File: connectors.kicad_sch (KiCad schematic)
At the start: 1 part, among them J1 USB_C_Receptacle_USB2.0_14P

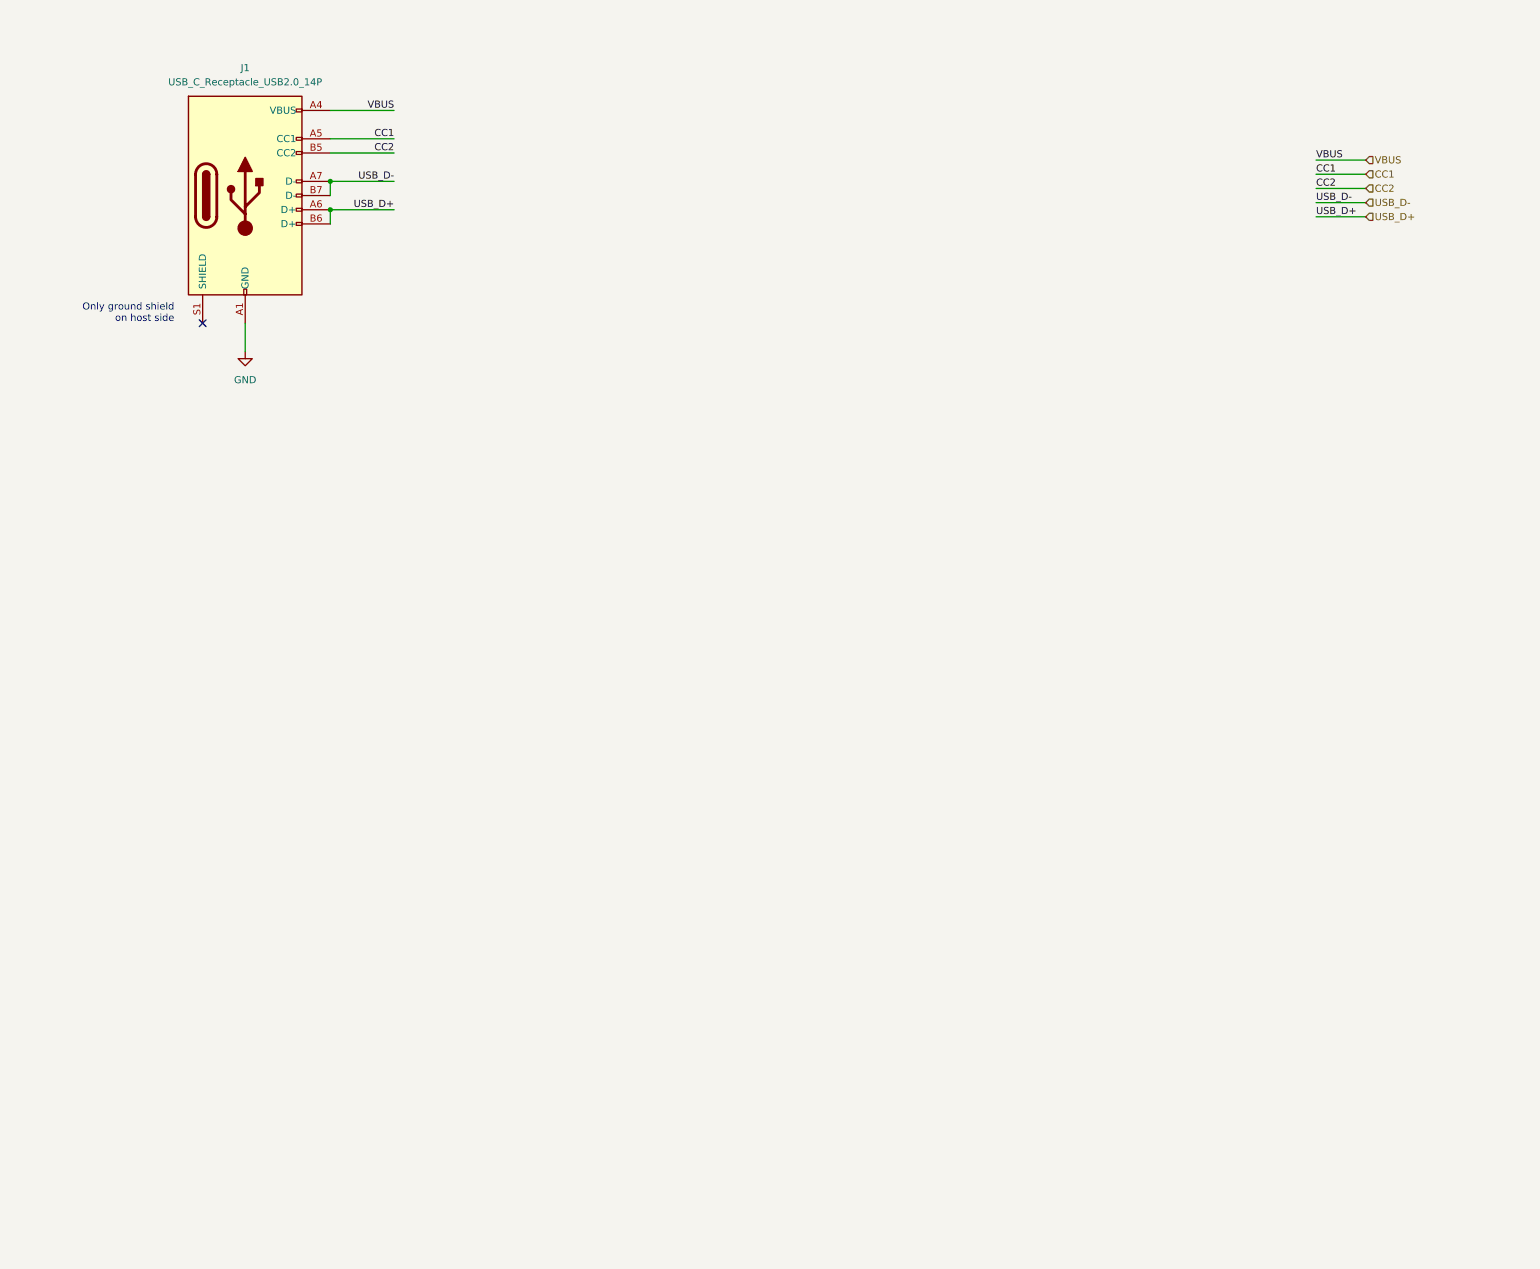
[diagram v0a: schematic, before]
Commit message: Add ESP32-S3-WROOM-1, 5V rail and UI sheet
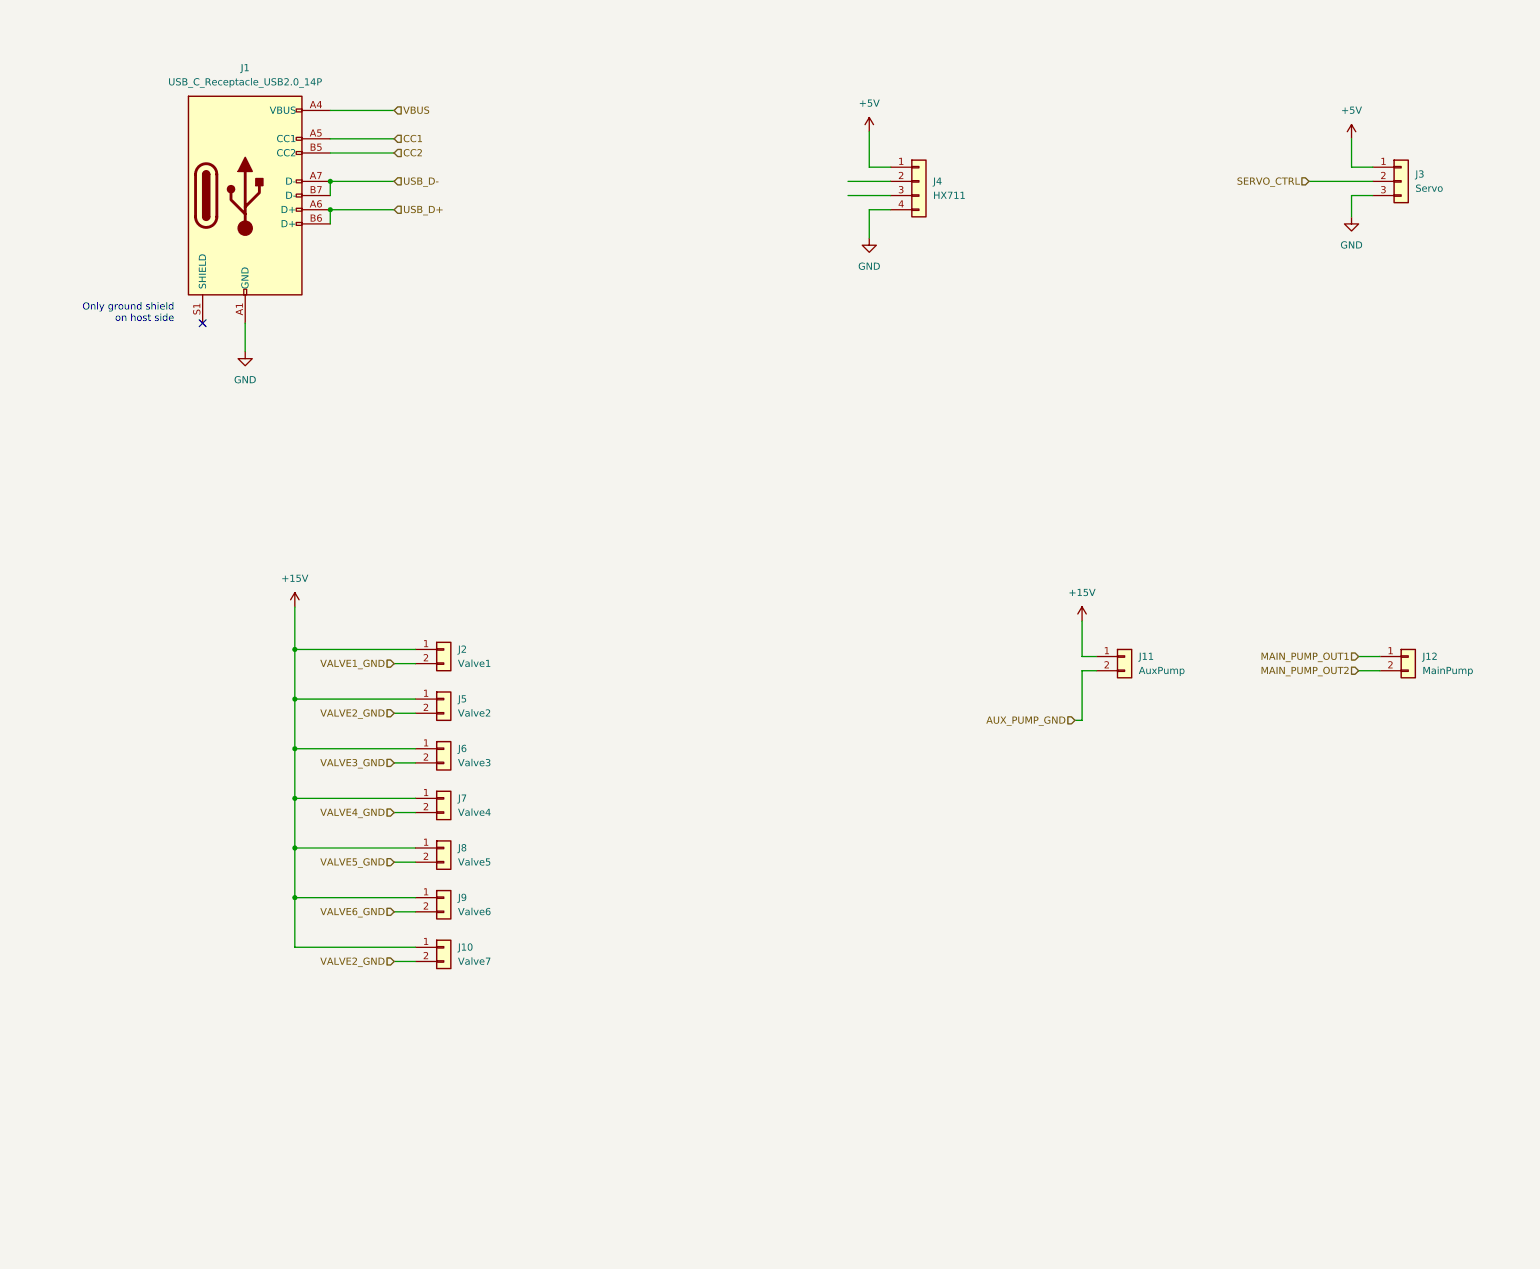
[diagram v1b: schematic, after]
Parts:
- added J10: Valve7, symbol Connector_Generic:Conn_01x02
- added J11: AuxPump, symbol Connector_Generic:Conn_01x02
- added J12: MainPump, symbol Connector_Generic:Conn_01x02
- added J2: Valve1, symbol Connector_Generic:Conn_01x02
- added J3: Servo, symbol Connector_Generic:Conn_01x03
- added J4: HX711, symbol Connector_Generic:Conn_01x04
- added J5: Valve2, symbol Connector_Generic:Conn_01x02
- added J6: Valve3, symbol Connector_Generic:Conn_01x02
- added J7: Valve4, symbol Connector_Generic:Conn_01x02
- added J8: Valve5, symbol Connector_Generic:Conn_01x02
- added J9: Valve6, symbol Connector_Generic:Conn_01x02
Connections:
- net GND: now also J3.3 (Pin_3), J4.4 (Pin_4)
- new net +15V: J10.1 (Pin_1), J11.1 (Pin_1), J2.1 (Pin_1), J5.1 (Pin_1), J6.1 (Pin_1), J7.1 (Pin_1), J8.1 (Pin_1), J9.1 (Pin_1)
- new net +5V: J3.1 (Pin_1), J4.1 (Pin_1)
- new net AUX_PUMP_GND: J11.2 (Pin_2)
- new net MAIN_PUMP_OUT1: J12.1 (Pin_1)
- new net MAIN_PUMP_OUT2: J12.2 (Pin_2)
- new net SERVO_CTRL: J3.2 (Pin_2)
- new net VALVE1_GND: J2.2 (Pin_2)
- new net VALVE2_GND: J10.2 (Pin_2), J5.2 (Pin_2)
- new net VALVE3_GND: J6.2 (Pin_2)
- new net VALVE4_GND: J7.2 (Pin_2)
- new net VALVE5_GND: J8.2 (Pin_2)
- new net VALVE6_GND: J9.2 (Pin_2)

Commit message: Finish first design
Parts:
- removed J1: USB_C_Receptacle_USB2.0_14P, symbol Connector:USB_C_Receptacle_USB2.0_14P
- added J1: USB_C_Receptacle_USB2.0_16P, project:USB_C_Receptacle_JAE_DX07S016JA1R1500, symbol Connector:USB_C_Receptacle_USB2.0_16P
- added J13: WaterLevelSensor, Connector_JST:JST_XH_B2B-XH-A_1x02_P2.50mm_Vertical, symbol Connector_Generic:Conn_01x02
- added J14: Conn_01x04, Connector_PinHeader_2.54mm:PinHeader_1x04_P2.54mm_Vertical, symbol Connector_Generic:Conn_01x04
- J10, J11, J12, J2, J5, J6, J7, J8, J9: footprint (none) -> Connector_JST:JST_XH_B2B-XH-A_1x02_P2.50mm_Vertical
- J3: footprint (none) -> Connector_JST:JST_XH_B3B-XH-A_1x03_P2.50mm_Vertical
- J4: footprint (none) -> Connector_JST:JST_XH_B4B-XH-A_1x04_P2.50mm_Vertical
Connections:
- net +15V: now also J13.1 (Pin_1)
- net CC1: now also J1.A5 (CC1)
- net CC2: now also J1.B5 (CC2)
- net GND: now also J1.A1 (GND), J1.A12 (GND), J1.B1 (GND), J1.B12 (GND), J1.S1 (SHIELD), J14.4 (Pin_4)
- net MAIN_PUMP_OUT1: now also J12.2 (Pin_2); no longer J12.1 (Pin_1)
- net MAIN_PUMP_OUT2: now also J12.1 (Pin_1); no longer J12.2 (Pin_2)
- net USB_D+: now also J1.A6 (D+), J1.B6 (D+)
- net USB_D-: now also J1.A7 (D-), J1.B7 (D-)
- net VALVE2_GND: no longer J10.2 (Pin_2)
- net VBUS: now also J1.A4 (VBUS), J1.A9 (VBUS), J1.B4 (VBUS), J1.B9 (VBUS)
- net HX711_CLK: now reaches J4.2 (Pin_2)
- net HX711_DAT: now reaches J4.3 (Pin_3)
- new net +3.3V: J14.1 (Pin_1)
- new net I2C_SCL: J14.3 (Pin_3)
- new net I2C_SDA: J14.2 (Pin_2)
- new net VALVE7_GND: J10.2 (Pin_2)
- new net WATER_LEVEL_SENSOR: J13.2 (Pin_2)
- no-connect marks 1 -> 2
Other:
- note added: "Check: OK"
- note added: "Check: TODO (shield)"
- note added: "I2C Display"
- note added: "Load Cell ADC (HX711) Datasheet: https://cdn.sparkfun.com/datasheets/Sensors/ForceFlex/hx711_english.pdf Current draw: ~ 2mA"
- note added: "Main / Aux. Pump Main pump peak current: ~ 0.6A Aux. pump peak current: ~ 0.7A"
- note added: "Peak Power: -> Two open valve, Main and aux. pump running, Servo active 15V (2 Valves, 2 Pumps): 600 + 600 + 600 + 700 = 3500mA -> 52.5W 5V (Servo, HX711): 800mA + 2mA = 802mA -> 4W 3.3V (MCU): 500mA -> 1.65W Total: 58.15W"
- note added: "Servo Motor Current draw: Idle: 10mA Movement: 120-250mA Stall: 800mA"
- note added: "USB-C PD Connection"
- note added: "Valves Peak current per valve at 15V: ~ 600mA L=21.5mH R=25R"
- note removed: "Only ground shield on host side"
- title: (none) -> openautolab - Mainboard
- moved on the sheet: J10, J11, J12, J2, J3, J4, J5, J6, J7, J8, J9
